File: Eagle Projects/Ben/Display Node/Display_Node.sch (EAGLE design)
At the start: 10 parts, among them Q1 16MHz, U1 ATMEGA328P_TQFP

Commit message: Working on PCB's and Generic CAN interface
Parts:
- added C3, C4: 22pF, resistor:C-EUC0805K
- added C5, C6: 100nF, resistor:C-EUC0805K
- added LED1: RX, led:LEDCHIP-LED0805
- added LED2: TX, led:LEDCHIP-LED0805
- added LED3: INT, led:LEDCHIP-LED0805
- added Q3: 16MHz, crystal:CRYSTALHC49S
- added Q4: 16MHz, crystal:CRYSTALHC49UP
- added R3, R4, R5: 1k, resistor:R-US_R0805
- added R6, R7: 100k, resistor:R-US_R0805
- added U$1: MCP2515SO, RobThePyro:MCP2515SO
- added U2: MCP2551, SparkFun:MCP2551
- added Z1, Z2: TVS-UD-SOD323, supressor:TVS-UD-SOD323
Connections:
- new net CANCS: U$1G$1.!CS
- new net CANH: U2.CANH, Z1.C
- new net CANINT: LED3.C, U$1G$1.!INT
- new net CANL: U2.CANL, Z2.C
- new net CANRST: R6.2, U$1G$1.!RESET
- new net CANSTBY: R7.1, U2.RS
- new net N$3: C3.1, Q3.2, Q4.2, U$1G$1.OSC1
- new net N$6: C4.1, Q3.1, Q4.1, U$1G$1.OSC2
- new net N$7: LED1.A, R3.1
- new net N$8: LED2.A, R4.1
- new net N$9: LED3.A, R5.1
- new net RXCAN: LED1.C, U$1G$1.RXCAN, U2.RXD
- new net TXCAN: LED2.C, U$1G$1.TXCAN, U2.TXD
- net +5V: now also C5.2, C6.2, R3.2, R4.2, R5.2, R6.1, U$1G$2.VDD, U2.VDD
- net GND: now also C3.2, C4.2, C5.1, C6.1, R7.2, U$1G$2.VSS, U2.VSS, Z1.A, Z2.A
- net MISO: now also U$1G$1.SO
- net MOSI: now also U$1G$1.SI
- net SCK: now also U$1G$1.SCK
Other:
- note added: "CAN Interface"

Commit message: Updates
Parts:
- removed JP2: CAN_Interface, pinhead:PINHD-1X4
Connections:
- removed net SS: JP2.1, U1.PB2(SS/OC1B)
- net CANCS: now also U1.PB2(SS/OC1B)
- net CANINT: now also U1.PB0(ICP)
- net LCD_CS: now also U1.PD7(AIN1); no longer U1.PB0(ICP)
- net MISO: no longer JP2.3
- net MOSI: no longer JP2.2
- net SCK: no longer JP2.4
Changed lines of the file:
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@@
 <part name="R2" library="resistor" deviceset="R-US_" device="R0805" value="1k"/>
 <part name="GND5" library="supply1" deviceset="GND" device=""/>
-<part name="JP2" library="pinhead" deviceset="PINHD-1X4" device="" value="CAN_Interface"/>
 <part name="JP1" library="atmel-avr" deviceset="AVR-ISP6-" device="75869-131" value="AVRISP6"/>
 <part name="GND6" library="supply1" deviceset="GND" device=""/>
@@
 <instance part="R2" gate="G$1" x="66.04" y="38.1" rot="R180"/>
 <instance part="GND5" gate="1" x="78.74" y="58.42" rot="R270"/>
-<instance part="JP2" gate="A" x="30.48" y="10.16" rot="R270"/>
 <instance part="JP1" gate="G$1" x="73.66" y="0" rot="R90"/>
 <instance part="GND6" gate="1" x="83.82" y="10.16" rot="R90"/>
@@
 </segment>
 <segment>
-<pinref part="JP2" gate="A" pin="2"/>
-<wire x1="33.02" y1="12.7" x2="33.02" y2="20.32" width="0.1524" layer="91"/>
-<label x="33.02" y="20.32" size="1.778" layer="95" rot="R90"/>
-</segment>
-<segment>
 <pinref part="JP1" gate="G$1" pin="4"/>
 <wire x1="76.2" y1="7.62" x2="76.2" y2="12.7" width="0.1524" layer="91"/>
@@
 </segment>
 <segment>
-<pinref part="JP2" gate="A" pin="4"/>
-<wire x1="27.94" y1="12.7" x2="27.94" y2="20.32" width="0.1524" layer="91"/>
-<label x="27.94" y="20.32" size="1.778" layer="95" rot="R90"/>
-</segment>
-<segment>
 <pinref part="JP1" gate="G$1" pin="3"/>
 <wire x1="73.66" y1="7.62" x2="73.66" y2="12.7" width="0.1524" layer="91"/>
@@
 </segment>
 <segment>
-<pinref part="JP2" gate="A" pin="3"/>
-<wire x1="30.48" y1="12.7" x2="30.48" y2="20.32" width="0.1524" layer="91"/>
-<label x="30.48" y="20.32" size="1.778" layer="95" rot="R90"/>
-</segment>
-<segment>
 <pinref part="JP1" gate="G$1" pin="1"/>
 <wire x1="68.58" y1="7.62" x2="68.58" y2="12.7" width="0.1524" layer="91"/>
@@
 </segment>
 </net>
-<net name="SS" class="0">
-<segment>
-<pinref part="U1" gate="U$1" pin="PB2(SS/OC1B)"/>
-<wire x1="2.54" y1="45.72" x2="7.62" y2="45.72" width="0.1524" layer="91"/>
-<label x="10.16" y="45.72" size="1.778" layer="95"/>
-</segment>
-<segment>
-<pinref part="JP2" gate="A" pin="1"/>
-<wire x1="35.56" y1="12.7" x2="35.56" y2="20.32" width="0.1524" layer="91"/>
-<label x="35.56" y="20.32" size="1.778" layer="95" rot="R90"/>
-</segment>
-</net>
 <net name="LCD_PWM" class="0">
 <segment>
@@
 <net name="LCD_CS" class="0">
 <segment>
-<pinref part="U1" gate="U$1" pin="PB0(ICP)"/>
-<wire x1="2.54" y1="50.8" x2="7.62" y2="50.8" width="0.1524" layer="91"/>
-<label x="10.16" y="50.8" size="1.778" layer="95"/>
-</segment>
-<segment>
 <pinref part="JP3" gate="A" pin="4"/>
 <wire x1="88.9" y1="86.36" x2="76.2" y2="86.36" width="0.1524" layer="91"/>
 <label x="71.12" y="86.36" size="1.778" layer="95"/>
+</segment>
+<segment>
+<pinref part="U1" gate="U$1" pin="PD7(AIN1)"/>
+<wire x1="2.54" y1="55.88" x2="7.62" y2="55.88" width="0.1524" layer="91"/>
+<label x="10.16" y="55.88" size="1.778" layer="95"/>
 </segment>
 </net>
@@
 <junction x="104.14" y="-86.36"/>
 </segment>
+<segment>
+<pinref part="U1" gate="U$1" pin="PB0(ICP)"/>
+<wire x1="2.54" y1="50.8" x2="7.62" y2="50.8" width="0.1524" layer="91"/>
+<label x="10.16" y="50.8" size="1.778" layer="95"/>
+</segment>
 </net>
 <net name="CANCS" class="0">
@@
 <label x="40.64" y="-73.66" size="1.778" layer="95"/>
 </segment>
-</net>
+<segment>
+<pinref part="U1" gate="U$1" pin="PB2(SS/OC1B)"/>
+<wire x1="2.54" y1="45.72" x2="7.62" y2="45.72" width="0.1524" layer="91"/>
+<label x="10.16" y="45.72" size="1.778" layer="95"/>
+</segment>
+</net>

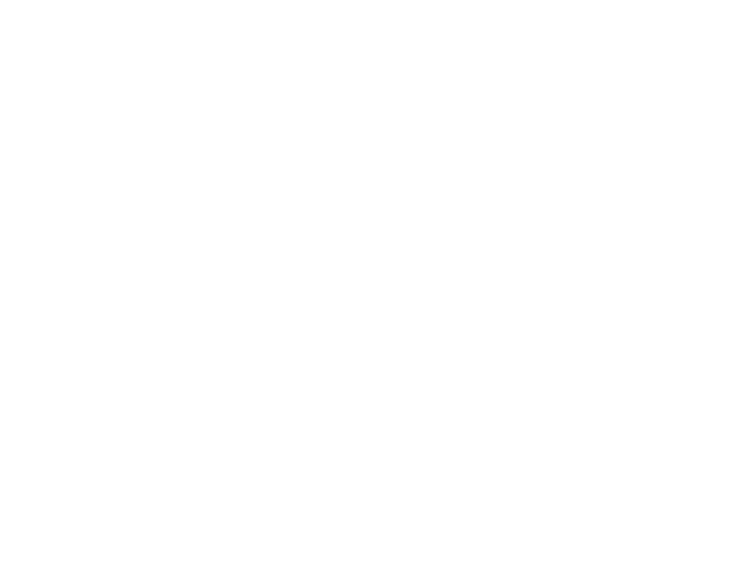
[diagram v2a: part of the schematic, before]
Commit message: Eagle Library RobThePyro with SMPS part added
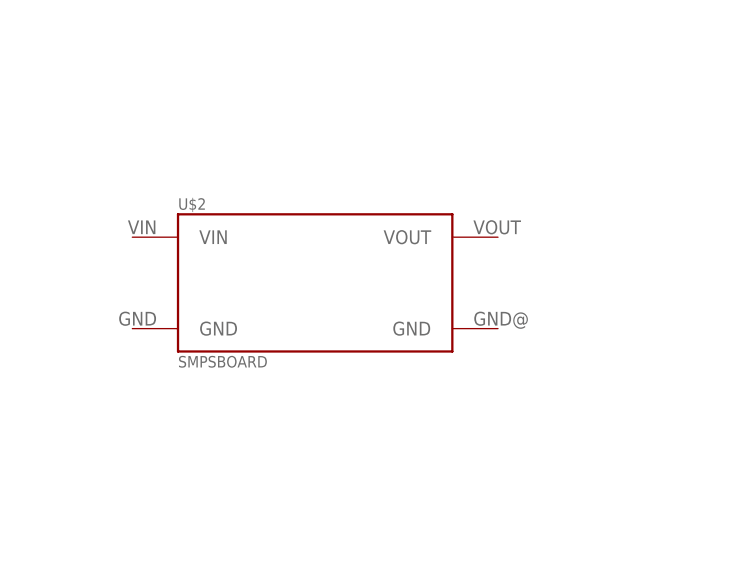
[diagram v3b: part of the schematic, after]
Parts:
- added U$2: SMPSBOARD, RobThePyro:SMPSBOARD
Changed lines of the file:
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@@
 <part name="Z2" library="supressor" deviceset="TVS-UD-" device="SOD323"/>
 <part name="GND10" library="supply1" deviceset="GND" device=""/>
+<part name="U$2" library="RobThePyro" deviceset="SMPSBOARD" device=""/>
 </parts>
 <sheets>
@@
 <instance part="Z2" gate="G$1" x="180.34" y="-93.98" rot="R90"/>
 <instance part="GND10" gate="1" x="177.8" y="-101.6"/>
+<instance part="U$2" gate="G$1" x="-35.56" y="-25.4"/>
 </instances>
 <busses>

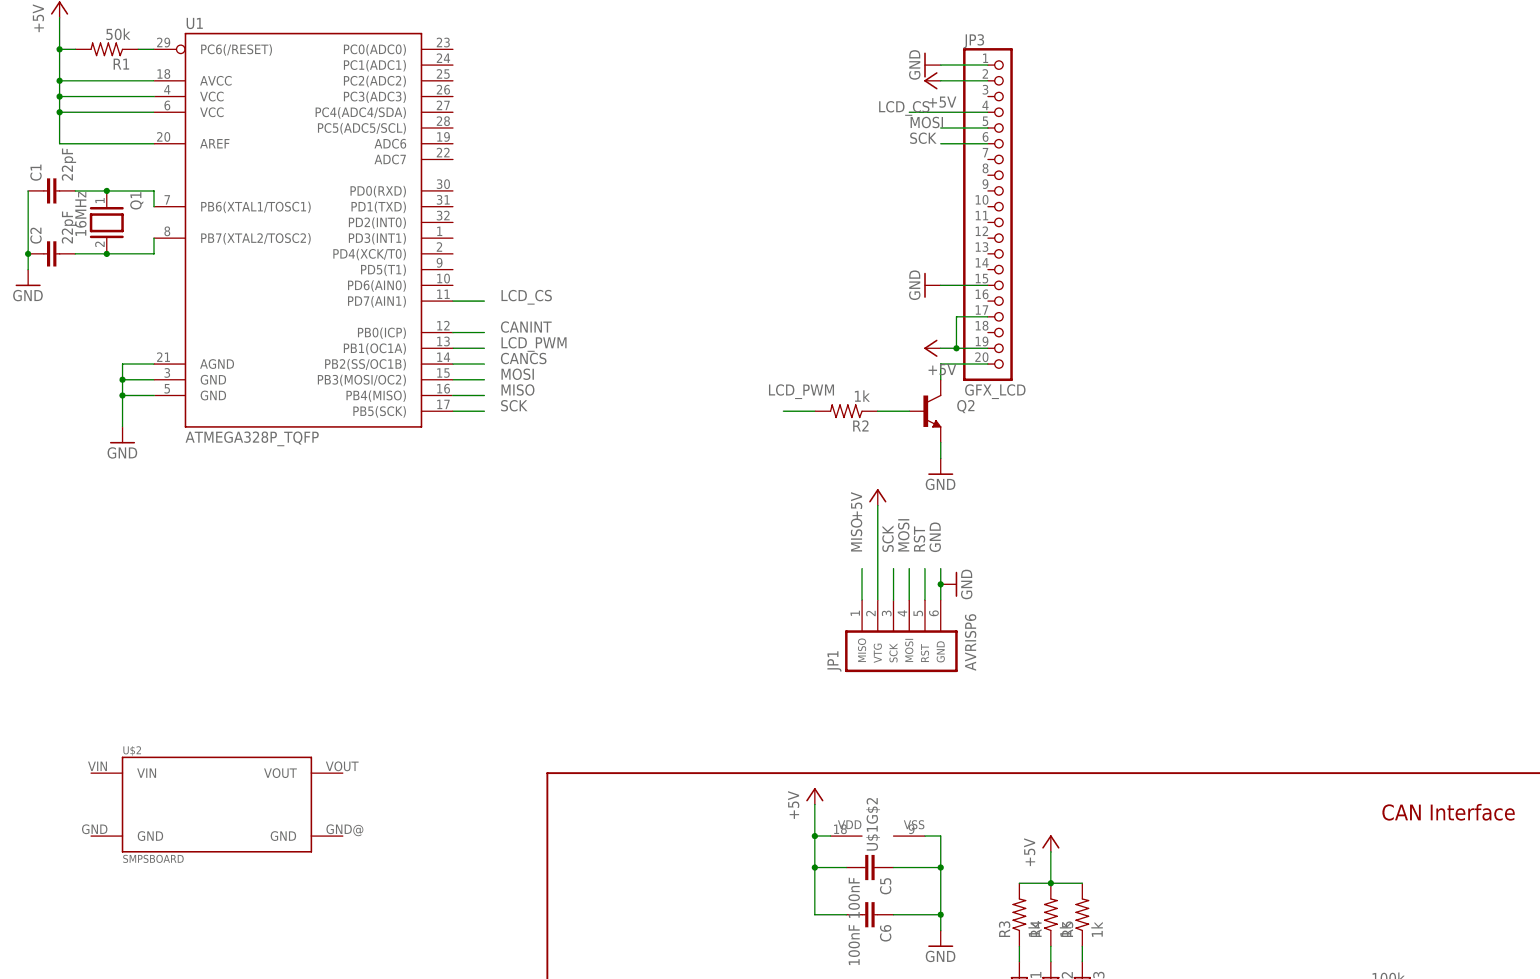
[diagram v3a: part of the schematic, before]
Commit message: Small change to library pin display
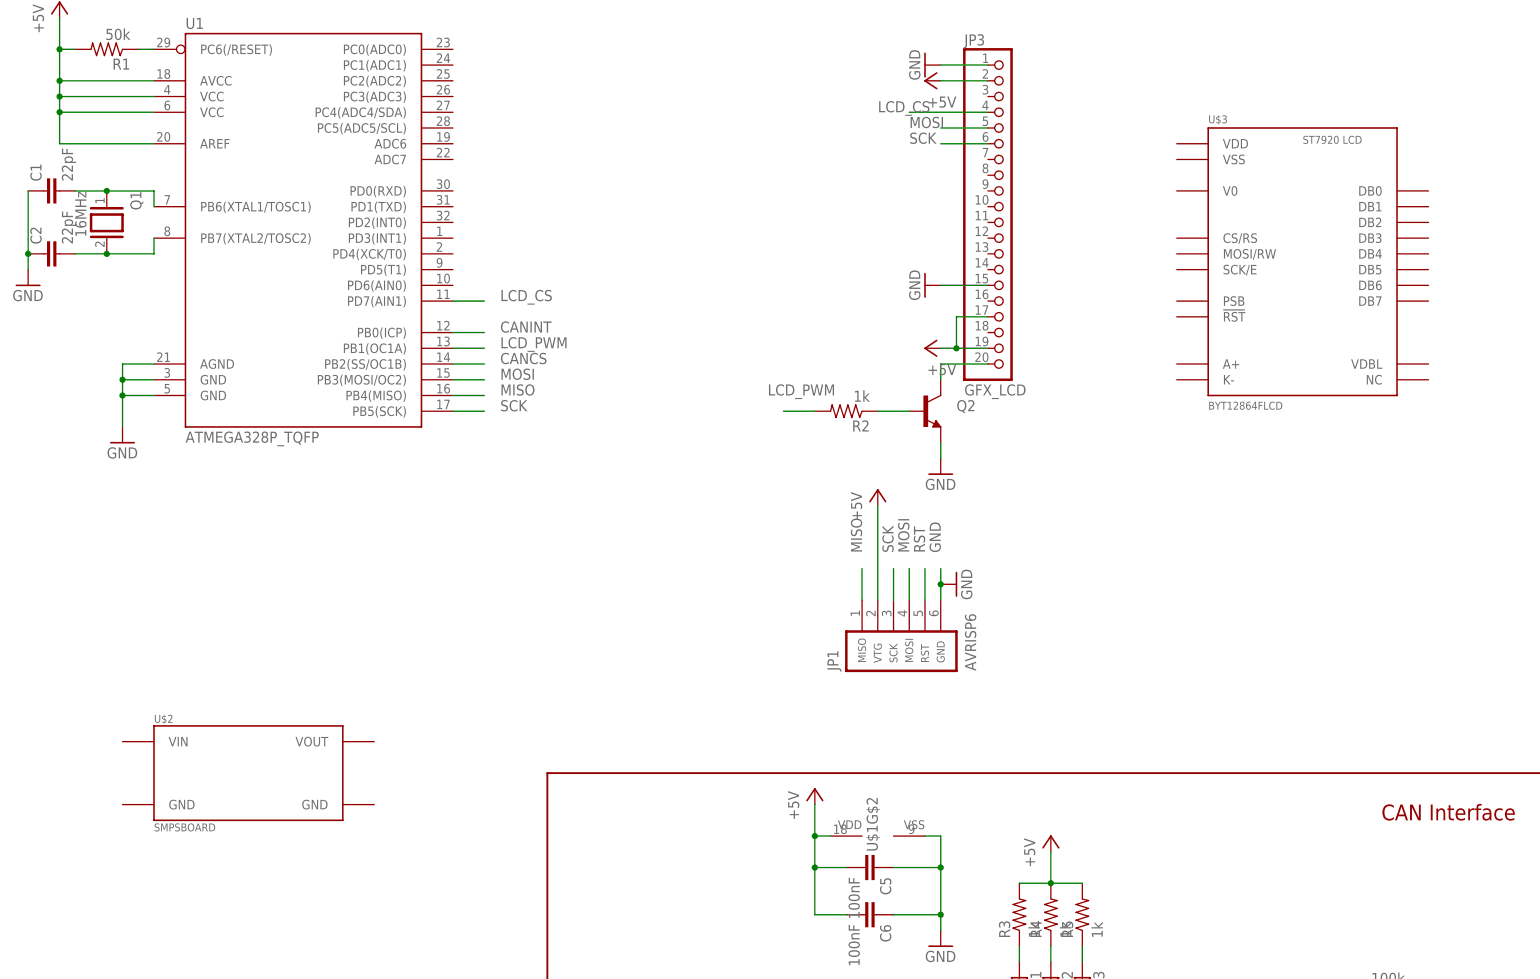
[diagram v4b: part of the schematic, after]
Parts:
- added U$3: BYT12864FLCD, RobThePyro:BYT12864FLCD
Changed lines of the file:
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@@
 <part name="Z2" library="supressor" deviceset="TVS-UD-" device="SOD323"/>
 <part name="GND10" library="supply1" deviceset="GND" device=""/>
+<part name="U$3" library="RobThePyro" deviceset="BYT12864FLCD" device=""/>
 <part name="U$2" library="RobThePyro" deviceset="SMPSBOARD" device=""/>
 </parts>
@@
 <instance part="Z2" gate="G$1" x="180.34" y="-93.98" rot="R90"/>
 <instance part="GND10" gate="1" x="177.8" y="-101.6"/>
-<instance part="U$2" gate="G$1" x="-35.56" y="-25.4"/>
+<instance part="U$3" gate="G$1" x="139.7" y="60.96"/>
+<instance part="U$2" gate="G$1" x="-30.48" y="-20.32"/>
 </instances>
 <busses>

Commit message: Workin on stuff...
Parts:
- removed JP3: GFX_LCD, adafruit:PINHD-1X20
- added X1, X2: 5566-6, con-molex:5566-6
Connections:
- new net +12V: U$2.VIN, X1-1.S, X2-1.S
- new net LCD_RST: U$3.!RST
- new net N$14: X1-5.S, X2-5.S
- new net N$15: X1-6.S, X2-6.S
- net +5V: now also U$2.VOUT, U$3.A+, U$3.VDD; no longer JP3.17, JP3.19, JP3.2
- net CANH: now also X1-3.S, X2-3.S
- net CANL: now also X1-4.S, X2-4.S
- net GND: now also U$2.GND, U$2.GND@1, U$3.PSB, U$3.VSS, X1-2.S, X2-2.S; no longer JP3.1, JP3.15
- net LCD_CS: now also U$3.CS/RS; no longer JP3.4
- net MOSI: now also U$3.MOSI/RW; no longer JP3.5
- net N$4: now also U$3.K-; no longer JP3.20
- net SCK: now also U$3.SCK/E; no longer JP3.6
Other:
- note added: "Power Supply"
- moved on the sheet: Q2, R2, U$2, U$3

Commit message: Almost lost some important stuff! managed to save it :D
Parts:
- added JP2: (no value), pinhead:PINHD-1X2
- added Q5: 16MHz, crystal:CRYSTALHC49UP
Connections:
- new net N$10: JP1.2, JP2.2
- net +12V: now also X1-3.S, X2-3.S; no longer X1-1.S, X2-1.S
- net +5V: now also JP2.1; no longer JP1.2
- net CANH: now also X1-1.S, X2-1.S; no longer X1-3.S, X2-3.S
- net N$1: now also Q5.2
- net N$2: now also Q5.1
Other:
- moved on the sheet: X1-1, X1-3, X2-1, X2-3
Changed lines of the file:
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@@
 <part name="X1" library="con-molex" deviceset="5566-6" device=""/>
 <part name="X2" library="con-molex" deviceset="5566-6" device=""/>
+<part name="JP2" library="pinhead" deviceset="PINHD-1X2" device=""/>
+<part name="Q5" library="crystal" deviceset="CRYSTAL" device="HC49UP" value="16MHz"/>
 </parts>
 <sheets>
@@
 <instance part="JP1" gate="G$1" x="73.66" y="0" rot="R90"/>
 <instance part="GND6" gate="1" x="83.82" y="10.16" rot="R90"/>
-<instance part="P+4" gate="1" x="71.12" y="25.4"/>
+<instance part="P+4" gate="1" x="71.12" y="35.56"/>
 <instance part="U$1" gate="G$1" x="76.2" y="-81.28"/>
 <instance part="U2" gate="G$1" x="147.32" y="-81.28"/>
@@
 <instance part="P+11" gate="1" x="76.2" y="182.88"/>
 <instance part="GND13" gate="1" x="81.28" y="172.72"/>
-<instance part="X1" gate="-1" x="91.44" y="177.8"/>
+<instance part="X1" gate="-1" x="91.44" y="167.64"/>
 <instance part="X1" gate="-2" x="91.44" y="175.26"/>
-<instance part="X1" gate="-3" x="91.44" y="167.64"/>
+<instance part="X1" gate="-3" x="91.44" y="177.8"/>
 <instance part="X1" gate="-4" x="91.44" y="165.1"/>
 <instance part="X1" gate="-5" x="91.44" y="157.48"/>
 <instance part="X1" gate="-6" x="91.44" y="154.94"/>
-<instance part="X2" gate="-1" x="106.68" y="177.8"/>
+<instance part="X2" gate="-1" x="106.68" y="167.64"/>
 <instance part="X2" gate="-2" x="106.68" y="175.26"/>
-<instance part="X2" gate="-3" x="106.68" y="167.64"/>
+<instance part="X2" gate="-3" x="106.68" y="177.8"/>
 <instance part="X2" gate="-4" x="106.68" y="165.1"/>
 <instance part="X2" gate="-5" x="106.68" y="157.48"/>
 <instance part="X2" gate="-6" x="106.68" y="154.94"/>
+<instance part="JP2" gate="G$1" x="73.66" y="25.4"/>
+<instance part="Q5" gate="G$1" x="-48.26" y="68.58" rot="R90"/>
 </instances>
 <busses>
@@
 <pinref part="Q1" gate="G$1" pin="1"/>
 <pinref part="U1" gate="U$1" pin="PB6(XTAL1/TOSC1)"/>
-<wire x1="-53.34" y1="73.66" x2="-45.72" y2="73.66" width="0.1524" layer="91"/>
+<wire x1="-53.34" y1="73.66" x2="-48.26" y2="73.66" width="0.1524" layer="91"/>
+<wire x1="-48.26" y1="73.66" x2="-45.72" y2="73.66" width="0.1524" layer="91"/>
 <wire x1="-45.72" y1="73.66" x2="-45.72" y2="71.12" width="0.1524" layer="91"/>
 <pinref part="C1" gate="G$1" pin="2"/>
 <wire x1="-58.42" y1="73.66" x2="-53.34" y2="73.66" width="0.1524" layer="91"/>
 <junction x="-53.34" y="73.66"/>
+<pinref part="Q5" gate="G$1" pin="2"/>
+<wire x1="-48.26" y1="71.12" x2="-48.26" y2="73.66" width="0.1524" layer="91"/>
+<junction x="-48.26" y="73.66"/>
 </segment>
 </net>
@@
 <pinref part="Q1" gate="G$1" pin="2"/>
 <pinref part="U1" gate="U$1" pin="PB7(XTAL2/TOSC2)"/>
-<wire x1="-53.34" y1="63.5" x2="-45.72" y2="63.5" width="0.1524" layer="91"/>
+<wire x1="-53.34" y1="63.5" x2="-48.26" y2="63.5" width="0.1524" layer="91"/>
+<wire x1="-48.26" y1="63.5" x2="-45.72" y2="63.5" width="0.1524" layer="91"/>
 <wire x1="-45.72" y1="63.5" x2="-45.72" y2="66.04" width="0.1524" layer="91"/>
 <pinref part="C2" gate="G$1" pin="2"/>
 <wire x1="-53.34" y1="63.5" x2="-58.42" y2="63.5" width="0.1524" layer="91"/>
 <junction x="-53.34" y="63.5"/>
+<pinref part="Q5" gate="G$1" pin="1"/>
+<wire x1="-48.26" y1="63.5" x2="-48.26" y2="66.04" width="0.1524" layer="91"/>
+<junction x="-48.26" y="63.5"/>
 </segment>
 </net>
@@
 </segment>
 <segment>
-<pinref part="JP1" gate="G$1" pin="2"/>
-<pinref part="P+4" gate="1" pin="+5V"/>
-<wire x1="71.12" y1="7.62" x2="71.12" y2="22.86" width="0.1524" layer="91"/>
-</segment>
-<segment>
 <pinref part="U2" gate="G$1" pin="VDD"/>
 <pinref part="P+6" gate="1" pin="+5V"/>
@@
 <wire x1="-10.16" y1="172.72" x2="-10.16" y2="175.26" width="0.1524" layer="91"/>
 </segment>
+<segment>
+<pinref part="JP2" gate="G$1" pin="1"/>
+<pinref part="P+4" gate="1" pin="+5V"/>
+<wire x1="71.12" y1="27.94" x2="71.12" y2="33.02" width="0.1524" layer="91"/>
+</segment>
 </net>
 <net name="N$4" class="0">
@@
 </segment>
 <segment>
-<pinref part="X2" gate="-3" pin="S"/>
-<pinref part="X1" gate="-3" pin="S"/>
+<pinref part="X2" gate="-1" pin="S"/>
+<pinref part="X1" gate="-1" pin="S"/>
 <wire x1="104.14" y1="167.64" x2="88.9" y2="167.64" width="0.1524" layer="91"/>
 <wire x1="88.9" y1="167.64" x2="76.2" y2="167.64" width="0.1524" layer="91"/>
@@
 <pinref part="P+11" gate="1" pin="+12V"/>
 <wire x1="76.2" y1="177.8" x2="76.2" y2="180.34" width="0.1524" layer="91"/>
-<pinref part="X2" gate="-1" pin="S"/>
-<pinref part="X1" gate="-1" pin="S"/>
+<pinref part="X2" gate="-3" pin="S"/>
+<pinref part="X1" gate="-3" pin="S"/>
 <wire x1="104.14" y1="177.8" x2="88.9" y2="177.8" width="0.1524" layer="91"/>
-<wire x1="88.9" y1="177.8" x2="76.2" y2="177.8" width="0.1524" layer="91"/>
+<wire x1="76.2" y1="177.8" x2="88.9" y2="177.8" width="0.1524" layer="91"/>
 <junction x="88.9" y="177.8"/>
 </segment>
@@
 </segment>
 </net>
+<net name="N$10" class="0">
+<segment>
+<pinref part="JP1" gate="G$1" pin="2"/>
+<pinref part="JP2" gate="G$1" pin="2"/>
+<wire x1="71.12" y1="7.62" x2="71.12" y2="25.4" width="0.1524" layer="91"/>
+</segment>
+</net>
